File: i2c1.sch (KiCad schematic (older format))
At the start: 3 parts, among them P10 I2C1_0, P11 I2C1_1, P12 I2C1_2

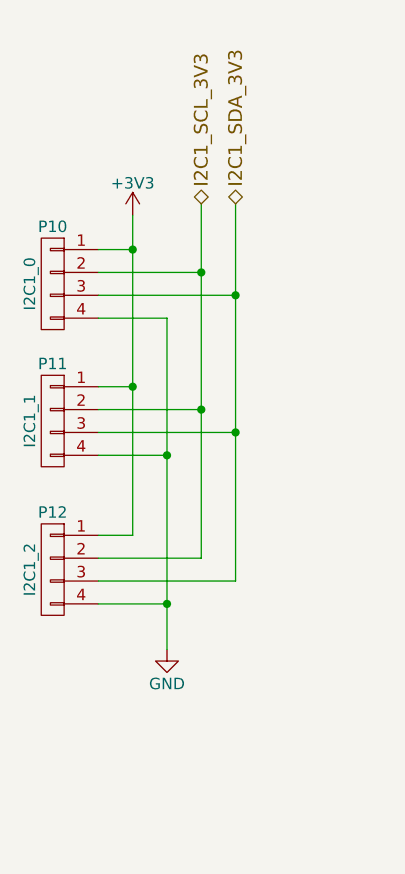
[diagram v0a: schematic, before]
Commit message: Deleted unnecessary files and splitting schmatics.
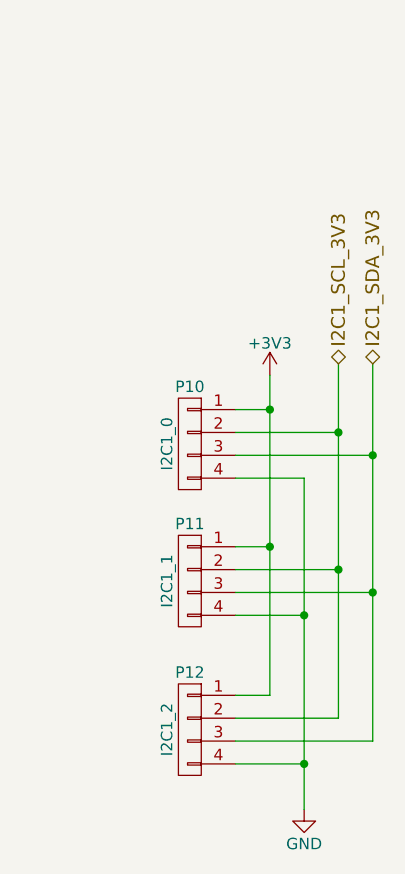
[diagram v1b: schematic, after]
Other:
- moved on the sheet: P10, P11, P12
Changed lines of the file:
@@
 $Descr A4 11693 8268
 encoding utf-8
-Sheet 6 6
-Title ""
+Sheet 6 8
+Title "DCoJA Yatagarasu Mezzanine"
 Date ""
 Rev ""
-Comp ""
-Comment1 ""
-Comment2 ""
-Comment3 ""
-Comment4 ""
+Comp "DroneWorks Inc."
+Comment1 "Copyright (c) 2016 DroneWorks Inc."
+Comment2 "All rights reserved."
+Comment3 "Creative Commons  (CC BY-SA 4.0)"
+Comment4 "Designed by: Michihiro Imaoka (@imaoca)"
 $EndDescr
-Text HLabel 5350 2250 1    60   BiDi ~ 0
+Text HLabel 5950 2950 1    60   BiDi ~ 0
 I2C1_SCL_3V3
-Text HLabel 5500 2250 1    60   BiDi ~ 0
+Text HLabel 6100 2950 1    60   BiDi ~ 0
 I2C1_SDA_3V3
 $Comp
 L CONN_01X04 P10
 U 1 1 56F7EFBA
-P 4700 2600
-F 0 "P10" H 4700 2850 50  0000 C CNN
-F 1 "I2C1_0" V 4800 2600 50  0000 C CNN
-F 2 "mylib:GH_4P_side" H 4700 2600 60  0001 C CNN
-F 3 "" H 4700 2600 60  0000 C CNN
-	1    4700 2600
+P 5300 3300
+F 0 "P10" H 5300 3550 50  0000 C CNN
+F 1 "I2C1_0" V 5400 3300 50  0000 C CNN
+F 2 "mylib:GH_4P_side" H 5300 3300 60  0001 C CNN
+F 3 "" H 5300 3300 60  0000 C CNN
+	1    5300 3300
 	-1   0    0    -1
 $EndComp
@@
 L CONN_01X04 P11
 U 1 1 56F7EFC1
-P 4700 3200
-F 0 "P11" H 4700 3450 50  0000 C CNN
-F 1 "I2C1_1" V 4800 3200 50  0000 C CNN
-F 2 "mylib:GH_4P_side" H 4700 3200 60  0001 C CNN
-F 3 "" H 4700 3200 60  0000 C CNN
-	1    4700 3200
+P 5300 3900
+F 0 "P11" H 5300 4150 50  0000 C CNN
+F 1 "I2C1_1" V 5400 3900 50  0000 C CNN
+F 2 "mylib:GH_4P_side" H 5300 3900 60  0001 C CNN
+F 3 "" H 5300 3900 60  0000 C CNN
+	1    5300 3900
 	-1   0    0    -1
 $EndComp
@@
 L CONN_01X04 P12
 U 1 1 56F7EFC8
-P 4700 3850
-F 0 "P12" H 4700 4100 50  0000 C CNN
-F 1 "I2C1_2" V 4800 3850 50  0000 C CNN
-F 2 "mylib:GH_4P_side" H 4700 3850 60  0001 C CNN
-F 3 "" H 4700 3850 60  0000 C CNN
-	1    4700 3850
+P 5300 4550
+F 0 "P12" H 5300 4800 50  0000 C CNN
+F 1 "I2C1_2" V 5400 4550 50  0000 C CNN
+F 2 "mylib:GH_4P_side" H 5300 4550 60  0001 C CNN
+F 3 "" H 5300 4550 60  0000 C CNN
+	1    5300 4550
 	-1   0    0    -1
 $EndComp
 $Comp
-L GND #PWR0104
+L GND #PWR092
 U 1 1 56F7EFD5
-P 5200 4200
-F 0 "#PWR0104" H 5200 3950 50  0001 C CNN
-F 1 "GND" H 5200 4050 50  0000 C CNN
-F 2 "" H 5200 4200 60  0000 C CNN
-F 3 "" H 5200 4200 60  0000 C CNN
-	1    5200 4200
+P 5800 4900
+F 0 "#PWR092" H 5800 4650 50  0001 C CNN
+F 1 "GND" H 5800 4750 50  0000 C CNN
+F 2 "" H 5800 4900 60  0000 C CNN
+F 3 "" H 5800 4900 60  0000 C CNN
+	1    5800 4900
 	-1   0    0    -1
 $EndComp
 Wire Wire Line
-	5350 2250 5350 3800
+	5950 2950 5950 4500
 Wire Wire Line
-	5500 2250 5500 3900
+	6100 2950 6100 4600
 Wire Wire Line
-	5350 3150 4900 3150
-Connection ~ 5350 2550
+	5950 3850 5500 3850
+Connection ~ 5950 3250
 Wire Wire Line
-	5350 3800 4900 3800
-Connection ~ 5350 3150
+	5950 4500 5500 4500
+Connection ~ 5950 3850
 Wire Wire Line
-	5500 3250 4900 3250
-Connection ~ 5500 2650
+	6100 3950 5500 3950
+Connection ~ 6100 3350
 Wire Wire Line
-	5500 3900 4900 3900
-Connection ~ 5500 3250
+	6100 4600 5500 4600
+Connection ~ 6100 3950
 Wire Wire Line
-	5050 2300 5050 3700
+	5650 3000 5650 4400
 Wire Wire Line
-	5050 2450 4900 2450
+	5650 3150 5500 3150
 Wire Wire Line
-	5050 3050 4900 3050
-Connection ~ 5050 2450
+	5650 3750 5500 3750
+Connection ~ 5650 3150
 Wire Wire Line
-	5050 3700 4900 3700
-Connection ~ 5050 3050
+	5650 4400 5500 4400
+Connection ~ 5650 3750
 Wire Wire Line
-	5200 2750 5200 4200
+	5800 3450 5800 4900
 Wire Wire Line
-	5200 4000 4900 4000
+	5800 4700 5500 4700
 Wire Wire Line
-	5200 3350 4900 3350
-Connection ~ 5200 4000
+	5800 4050 5500 4050
+Connection ~ 5800 4700
 Wire Wire Line
-	5200 2750 4900 2750
-Connection ~ 5200 3350
+	5800 3450 5500 3450
+Connection ~ 5800 4050
 Wire Wire Line
-	4900 2550 5350 2550
+	5500 3250 5950 3250
 $Comp
-L +3V3 #PWR0105
+L +3V3 #PWR093
 U 1 1 5707745E
-P 5050 2300
-F 0 "#PWR0105" H 5050 2150 50  0001 C CNN
-F 1 "+3V3" H 5050 2440 50  0000 C CNN
-F 2 "" H 5050 2300 50  0000 C CNN
-F 3 "" H 5050 2300 50  0000 C CNN
-	1    5050 2300
+P 5650 3000
+F 0 "#PWR093" H 5650 2850 50  0001 C CNN
+F 1 "+3V3" H 5650 3140 50  0000 C CNN
+F 2 "" H 5650 3000 50  0000 C CNN
+F 3 "" H 5650 3000 50  0000 C CNN
+	1    5650 3000
 	1    0    0    -1
 $EndComp
 Wire Wire Line
-	5500 2650 4900 2650
+	6100 3350 5500 3350
 $EndSCHEMATC
